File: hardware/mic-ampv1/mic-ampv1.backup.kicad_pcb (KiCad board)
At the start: 2 copper layers, 18 parts, among them U1 NE5532

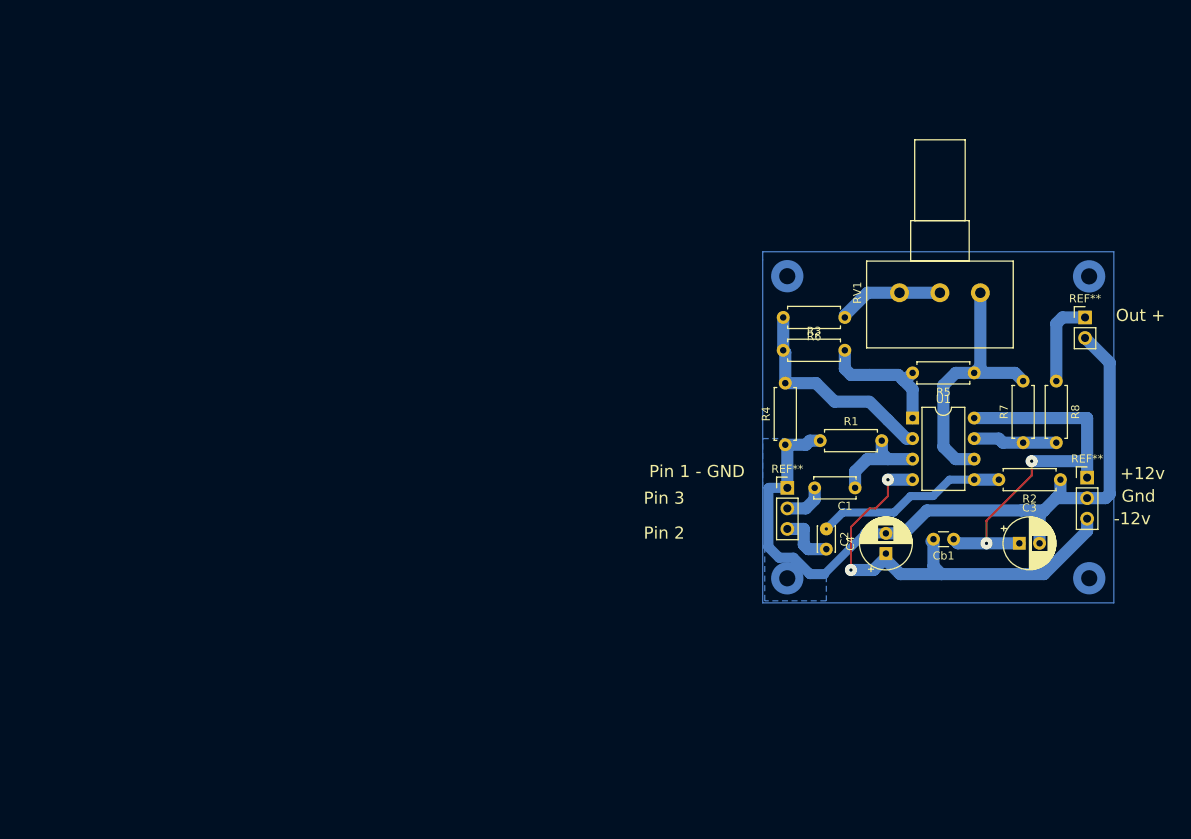
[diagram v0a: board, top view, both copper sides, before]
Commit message: complete pcb for mic
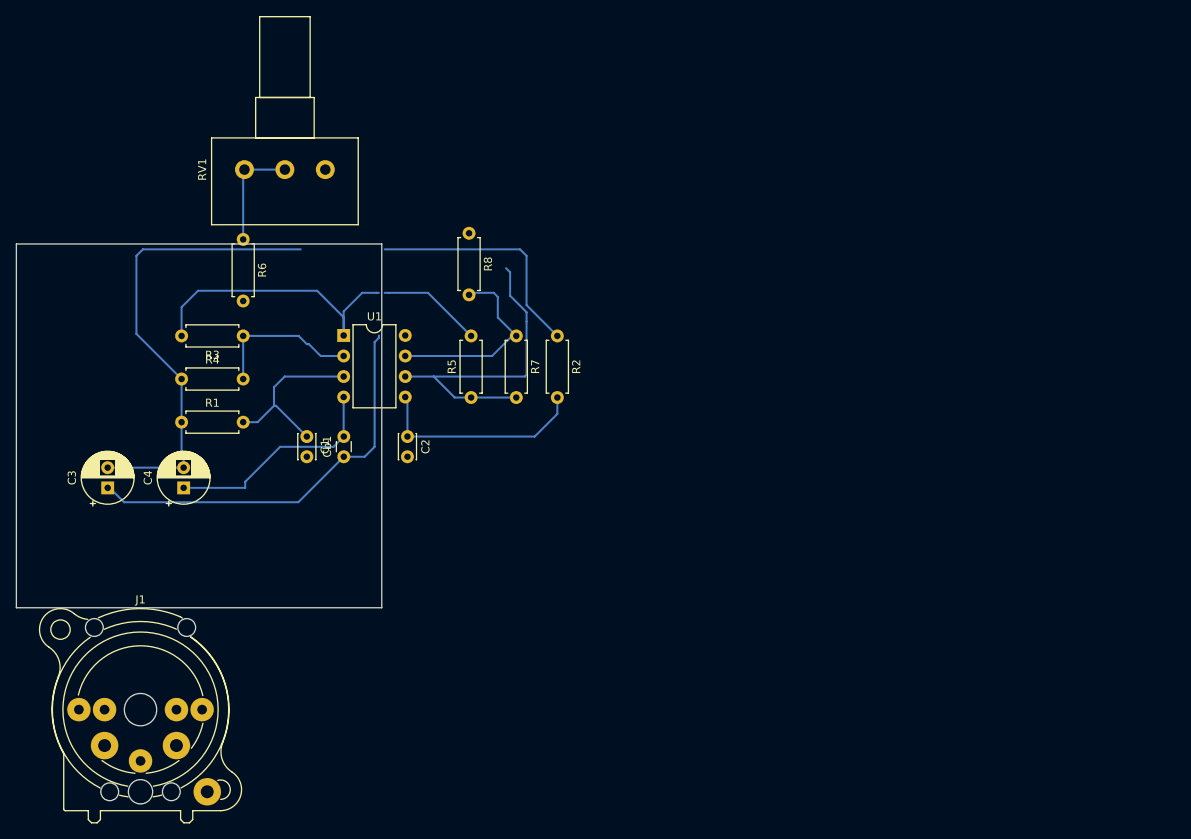
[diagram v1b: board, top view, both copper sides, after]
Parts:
- removed REF** (x2): PinHeader_1x03_P2.54mm_Vertical, Connector_PinHeader_2.54mm:PinHeader_1x03_P2.54mm_Vertical
- removed REF**: PinHeader_1x02_P2.54mm_Vertical, Connector_PinHeader_2.54mm:PinHeader_1x02_P2.54mm_Vertical
- added J1: XLR3_Switched, Connector_Audio:Jack_XLR-6.35mm_Neutrik_NCJ6FA-V-0_Vertical, F.Cu at (103.4, 117.6)
- C1: footprint Capacitor_THT:C_Disc_D5.0mm_W2.5mm_P5.00mm -> Capacitor_THT:C_Disc_D3.0mm_W2.0mm_P2.50mm
- moved C3 113.0 mm to (91.7, 90.2), turned to 90 degrees
- moved C4 87.2 mm to (101.1, 90.2)
- moved RV1 82.4 mm to (118.6, 50.8)
- moved R1 79.0 mm to (100.8, 82.0)
- moved Cb1 76.1 mm to (120.9, 86.3), turned to 90 degrees
- moved R4 75.1 mm to (100.8, 76.7), turned to 0 degrees
- moved R6 75.0 mm to (108.5, 59.4), turned to 270 degrees
- moved R8 74.9 mm to (136.4, 58.7)
- moved U1 71.1 mm to (120.9, 71.3)
- moved C1 68.1 mm to (116.3, 83.8), turned to 270 degrees
- moved R3 66.8 mm to (108.5, 71.4), turned to 180 degrees
- moved R2 64.7 mm to (147.3, 71.4), turned to 270 degrees
- moved R7 64.1 mm to (142.2, 71.4), turned to 270 degrees
- moved R5 62.3 mm to (136.7, 79.0), turned to 90 degrees
- moved C2 53.1 mm to (128.8, 83.8)
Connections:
- net Gnd renamed GND
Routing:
- net Net-(R3-Pad2): track 16.8 -> 49.3 mm
- net -12V: track 57.2 -> 27.8 mm, vias 2 -> 0
- net Net-(R7-Pad1): track 10.4 -> 24.4 mm
- net (no net): track 11.0 -> 0.00 mm
- net Net-(C1-Pad1): track 12.4 -> 21.7 mm
- net GND: track 97.7 -> 88.4 mm
- net Net-(R3-Pad1): track 26.8 -> 18.8 mm
- net Net-(R5-Pad1): track 33.2 -> 40.6 mm
- net Net-(C1-Pad2): track 7.06 -> 0.00 mm
- net Net-(C2-Pad2): track 7.00 -> 0.00 mm
- net Net-(C2-Pad1): track 23.9 -> 26.7 mm
- net +12V: track 49.1 -> 50.6 mm, vias 2 -> 0
- net Net-(R6-Pad1): track 13.2 -> 13.7 mm
- removed copper zone on B.Cu, net GND
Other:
- board outline added: 45.2 x 45 mm
- board text removed: "+12v"
- board text removed: "-12v"
- board text removed: "Gnd"
- board text removed: "Out +"
- board text removed: "Pin 1 - GND"
- board text removed: "Pin 2"
- board text removed: "Pin 3"
